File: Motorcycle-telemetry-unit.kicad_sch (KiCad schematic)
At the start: 99 parts, among them J1 USB_B_Micro-ESP32, J2 Screw_Terminal_01x02, J3 Screw_Terminal_01x02, J4 Micro_SD_Card_Det, J5 GoPro Power USBAx2, J6 Screw_Terminal_01x10, K1 ADW11, SW1 RESET, U1 VO615A, U10 BNO085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

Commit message: Fixes and updates
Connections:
- net 5v-LED-CATH: now reaches D4.1 (K), R42.2
- net 3.3v-LED-CATH: now reaches D6.1 (K), R44.2
- net 12v-LED-CAT renamed 12v-LED-CATH
- net 5v-In renamed 5v-IN
- net CHARGING-LED-CAT renamed CHARGING-LED-CATH
- no-connect marks 19 -> 35
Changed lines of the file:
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@@
 (kicad_sch (version 20211123) (generator eeschema)
   (paper "A4")
+  (bus_alias "INPUT" (members ))
   (junction (at 272.415 160.655) (diameter 0) (color 0 0 0 0)
   )
@@
   (no_connect (at 118.745 138.43))
   (no_connect (at 128.905 138.43))
+  (no_connect (at 92.71 73.025))
+  (no_connect (at 92.71 75.565))
+  (no_connect (at 92.71 78.105))
+  (no_connect (at 92.71 83.185))
+  (no_connect (at 92.71 80.645))
+  (no_connect (at 123.19 34.925))
+  (no_connect (at 123.19 50.165))
+  (no_connect (at 123.19 52.705))
+  (no_connect (at 123.19 67.945))
+  (no_connect (at 123.19 70.485))
+  (no_connect (at 123.19 73.025))
+  (no_connect (at 123.19 37.465))
+  (no_connect (at 123.19 40.005))
+  (no_connect (at 123.19 42.545))
+  (no_connect (at 123.19 45.085))
+  (no_connect (at 123.19 47.625))
   (bus_entry (at 127 60.325) (size 2.54 2.54)
     (stroke (width 0) (type default) (color 0 0 0 0))
@@
     (stroke (width 0) (type default) (color 0 0 0 0))
   )
+  (polyline (pts (xy 243.205 87.63) (xy 246.38 87.63))
+    (stroke (width 0) (type default) (color 0 0 0 0))
+  )
   (wire (pts (xy 83.82 57.785) (xy 92.71 57.785))
     (stroke (width 0) (type default) (color 0 0 0 0))
@@
     (stroke (width 0) (type default) (color 0 0 0 0))
   )
+  (polyline (pts (xy 246.38 53.34) (xy 246.38 87.63))
+    (stroke (width 0) (type default) (color 0 0 0 0))
+  )
   (bus (pts (xy 69.215 115.57) (xy 69.215 133.35))
     (stroke (width 0) (type default) (color 0 0 0 0))
@@
     (stroke (width 0) (type default) (color 0 0 0 0))
   )
+  (bus (pts (xy 69.215 7.62) (xy 69.215 26.67))
+    (stroke (width 0) (type default) (color 0 0 0 0))
+  )
   (polyline (pts (xy 12.7 12.7) (xy 69.85 12.7))
     (stroke (width 0) (type default) (color 0 0 0 0))
@@
     (effects (font (size 1.27 1.27)) (justify left bottom))
   )
-  (label "I2C ENV" (at 157.48 147.32 0)
+  (label "{E_SDA E_SCL}" (at 157.48 147.32 0)
     (effects (font (size 1.27 1.27)) (justify left bottom))
   )
@@
     (effects (font (size 1.27 1.27)) (justify right bottom))
   )
-  (label "SPI" (at 129.54 67.945 0)
-    (effects (font (size 1.27 1.27)) (justify left bottom))
-  )
   (label "NEUTRAL" (at 58.42 130.81 0)
     (effects (font (size 1.27 1.27)) (justify left bottom))
@@
     (effects (font (size 1.27 1.27)) (justify left bottom))
   )
-  (label "I2C_HOST" (at 81.28 93.98 0)
-    (effects (font (size 1.27 1.27)) (justify left bottom))
-  )
   (label "NEUTRAL" (at 92.71 52.705 180)
     (effects (font (size 1.27 1.27)) (justify right bottom))
@@
     (effects (font (size 1.27 1.27)) (justify right bottom))
   )
-  (label "5v-In" (at 207.645 75.565 180)
+  (label "5v-IN" (at 207.645 75.565 180)
     (effects (font (size 1.27 1.27)) (justify right bottom))
   )
@@
     (effects (font (size 1.27 1.27)) (justify left bottom))
   )
-  (label "12v-LED-CAT" (at 280.035 74.295 0)
+  (label "12v-LED-CATH" (at 280.035 74.295 0)
     (effects (font (size 1.27 1.27)) (justify left bottom))
   )
@@
     (effects (font (size 1.27 1.27)) (justify right bottom))
   )
+  (label "{SD_DET MISO CLK MOSI SS1}" (at 191.135 95.885 180)
+    (effects (font (size 1.27 1.27)) (justify right bottom))
+  )
   (label "BR_REAR" (at 92.71 40.005 180)
     (effects (font (size 1.27 1.27)) (justify right bottom))
@@
     (effects (font (size 1.27 1.27)) (justify left bottom))
   )
-  (label "3.3v-Out" (at 225.425 73.025 0)
+  (label "3.3v-OUT" (at 225.425 73.025 0)
     (effects (font (size 1.27 1.27)) (justify left bottom))
   )
@@
     (effects (font (size 1.27 1.27)) (justify left bottom))
   )
+  (label "3.3v-LED-CATH" (at 280.035 34.29 0)
+    (effects (font (size 1.27 1.27)) (justify left bottom))
+  )
   (label "SS1" (at 211.455 116.84 90)
     (effects (font (size 1.27 1.27)) (justify left bottom))
   )
+  (label "{BR_FRNT BR_REAR TR_LEFT TR_RIGT IGN START NEUTRAL KICK TACH BIKE_BATT}"
+    (at 69.215 7.62 0)
+    (effects (font (size 1.27 1.27)) (justify left bottom))
+  )
   (label "MOSI" (at 123.19 62.865 0)
     (effects (font (size 1.27 1.27)) (justify left bottom))
@@
     (effects (font (size 1.27 1.27)) (justify right bottom))
   )
-  (label "CHARGING-LED-CAT" (at 271.145 74.295 180)
+  (label "CHARGING-LED-CATH" (at 271.145 74.295 180)
     (effects (font (size 1.27 1.27)) (justify right bottom))
   )
@@
     (effects (font (size 1.27 1.27)) (justify right bottom))
   )
+  (label "5v-LED-CATH" (at 270.51 34.29 180)
+    (effects (font (size 1.27 1.27)) (justify right bottom))
+  )
   (label "E_SCL" (at 162.56 137.795 270)
     (effects (font (size 1.27 1.27)) (justify right bottom))
@@
     (effects (font (size 1.27 1.27)) (justify right bottom))
   )
+  (label "{H_SDA H_SCL}" (at 81.28 93.98 0)
+    (effects (font (size 1.27 1.27)) (justify left bottom))
+  )
   (label "SD_DET" (at 123.19 55.245 0)
     (effects (font (size 1.27 1.27)) (justify left bottom))
@@
     (effects (font (size 1.27 1.27)) (justify left bottom))
   )
-  (label "Inputs" (at 71.755 43.815 0)
-    (effects (font (size 1.27 1.27)) (justify left bottom))
-  )
   (label "START" (at 58.42 113.03 0)
     (effects (font (size 1.27 1.27)) (justify left bottom))
@@
     (pin "1")
   )
-  (sheet (at 263.525 170.815) (size 12.7 6.35) (fields_autoplaced)
+  (sheet (at 229.235 85.09) (size 12.7 6.35) (fields_autoplaced)
     (stroke (width 0.1524) (type solid) (color 0 0 0 0))
     (fill (color 0 0 0 0.0000))
-    (property "Sheet name" "Charging H-Bridge" (id 0) (at 263.525 170.1034 0)
+    (property "Sheet name" "Charging H-Bridge" (id 0) (at 229.235 84.3784 0)
       (effects (font (size 1.27 1.27)) (justify left bottom))
     )
-    (property "Sheet file" "charging_h-bridge.kicad_sch" (id 1) (at 263.525 177.7496 0)
+    (property "Sheet file" "charging_h-bridge.kicad_sch" (id 1) (at 229.235 92.0246 0)
       (effects (font (size 1.27 1.27)) (justify left top))
     )

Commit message: More clean up
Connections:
- net HOST_INT: now also U11.18 (IO15)
- net ANT.: now reaches AE1.1 (A), U12.11 (RF_IN)
- net IMU_BOOTN: now reaches U11.17 (IO14)
- net IMU_BOOTN: now also U10.4 (BOOTN)
- net Charge-Sens renamed 5V-OUT
- no-connect marks 35 -> 50
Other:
- moved on the sheet: R37, R38

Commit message: wired
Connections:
- net +5V: no longer J5.1 (VBUS1), J5.5 (VBUS2)
- net 5V-OUT: now also J5.1 (VBUS1), J5.5 (VBUS2)
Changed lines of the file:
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@@
   (junction (at 50.8 113.03) (diameter 0) (color 0 0 0 0)
   )
-  (junction (at 282.575 135.255) (diameter 0) (color 0 0 0 0)
-  )
   (junction (at 140.97 93.98) (diameter 0) (color 0 0 0 0)
   )
@@
     (effects (font (size 1.27 1.27)) (justify left bottom))
   )
+  (label "5V-OUT" (at 282.575 135.255 90)
+    (effects (font (size 1.27 1.27)) (justify left bottom))
+  )
   (label "NEUTRAL" (at 92.71 52.705 180)
     (effects (font (size 1.27 1.27)) (justify right bottom))
@@
     (pin "2")
   )
-  (symbol (lib_id "power:+5V") (at 282.575 135.255 0) (unit 1)
-    (in_bom yes) (on_board yes) (fields_autoplaced)
-    (property "Reference" "#PWR084" (id 0) (at 282.575 139.065 0)
-      (effects (font (size 1.27 1.27)) hide)
-    )
-    (property "Value" "+5V" (id 1) (at 282.575 131.6505 0))
-    (property "Footprint" "" (id 2) (at 282.575 135.255 0)
-      (effects (font (size 1.27 1.27)) hide)
-    )
-    (property "Datasheet" "" (id 3) (at 282.575 135.255 0)
-      (effects (font (size 1.27 1.27)) hide)
-    )
-    (pin "1")
-  )
   (symbol (lib_id "power:GND") (at 280.035 79.375 0) (unit 1)
     (in_bom yes) (on_board yes)
@@
       (reference "#PWR083") (unit 1) (value "GND") (footprint "")
     )
-    (path "/d3319a11-c2a0-4905-b28a-862dc66a010f"
-      (reference "#PWR084") (unit 1) (value "+5V") (footprint "")
-    )
     (path "/97e5f366-bed2-49ed-8e99-850598d1913a"

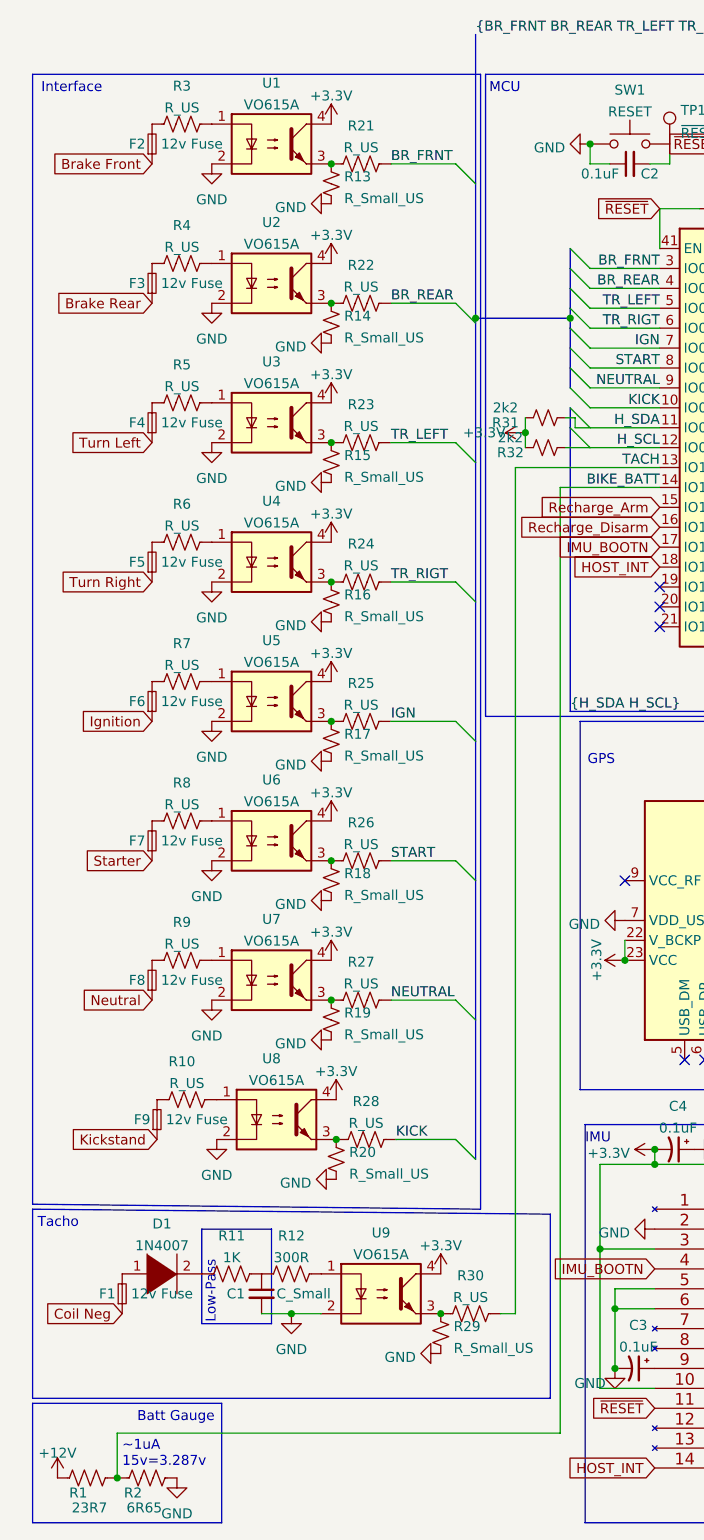
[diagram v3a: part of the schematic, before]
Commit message: Corrections to optoarray
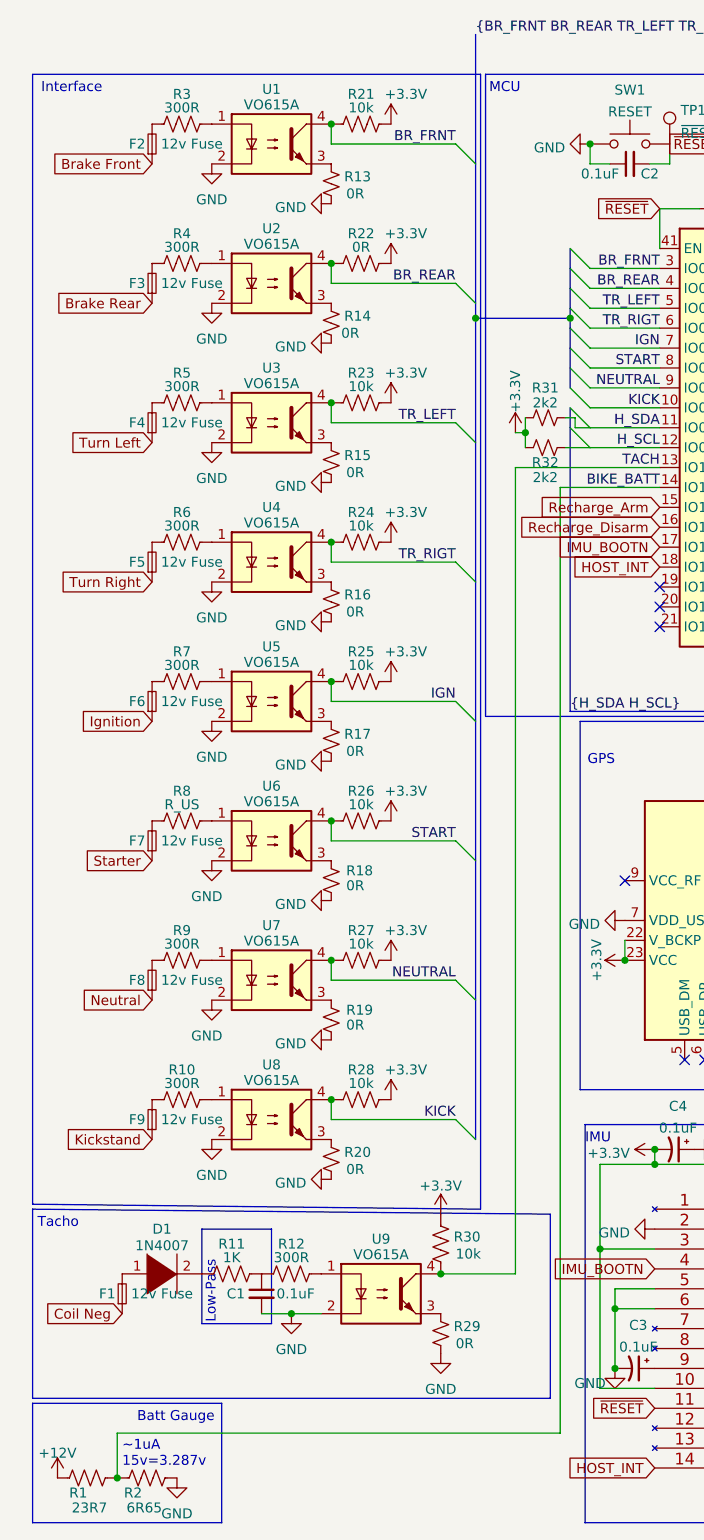
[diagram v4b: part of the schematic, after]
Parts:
- C1: value C_Small -> 0.1uF
- R10, R3, R4, R5, R6, R7, R9: value R_US -> 300R
- R13, R14, R15, R16, R17, R18, R19, R20, R29: value R_Small_US -> 0R
- R21, R23, R24, R25, R26, R27, R28, R30: value R_US -> 10k
- R22: value R_US -> 0R
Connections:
- net +3V3: now also R21.2, R22.2, R23.2, R24.2, R25.2, R26.2, R27.2, R28.2, R30.2; no longer U1.4, U2.4, U3.4, U4.4, U5.4, U6.4, U7.4, U8.4, U9.4
- net BR_FRNT: now also R21.1, U1.4; no longer R21.2
- net BR_REAR: now also R22.1, U2.4; no longer R22.2
- net IGN: now also R25.1, U5.4; no longer R25.2
- net KICK: now also R28.1, U8.4; no longer R28.2
- net NEUTRAL: now also R27.1, U7.4; no longer R27.2
- net START: now also R26.1, U6.4; no longer R26.2
- net TACH: now also R30.1, U9.4; no longer R30.2
- net TR_LEFT: now also R23.1, U3.4; no longer R23.2
- net TR_RIGT: now also R24.1, U4.4; no longer R24.2
- net at R14.1, U2.3: no longer R22.1
- net at R17.1, U5.3: no longer R25.1
- net at R29.1, U9.3: no longer R30.1
- net at R20.1, U8.3: no longer R28.1
- net at R19.1, U7.3: no longer R27.1
- net at R18.1, U6.3: no longer R26.1
- net at R13.1, U1.3: no longer R21.1
- net at R16.1, U4.3: no longer R24.1
- net at R15.1, U3.3: no longer R23.1
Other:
- moved on the sheet: F9, R10, R20, R21, R22, R23, R24, R25, R26, R27, R28, R30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
